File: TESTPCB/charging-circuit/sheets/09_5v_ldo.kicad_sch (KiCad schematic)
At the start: 8 parts, among them P6 1.27mm/1*3p, U2 MT3608

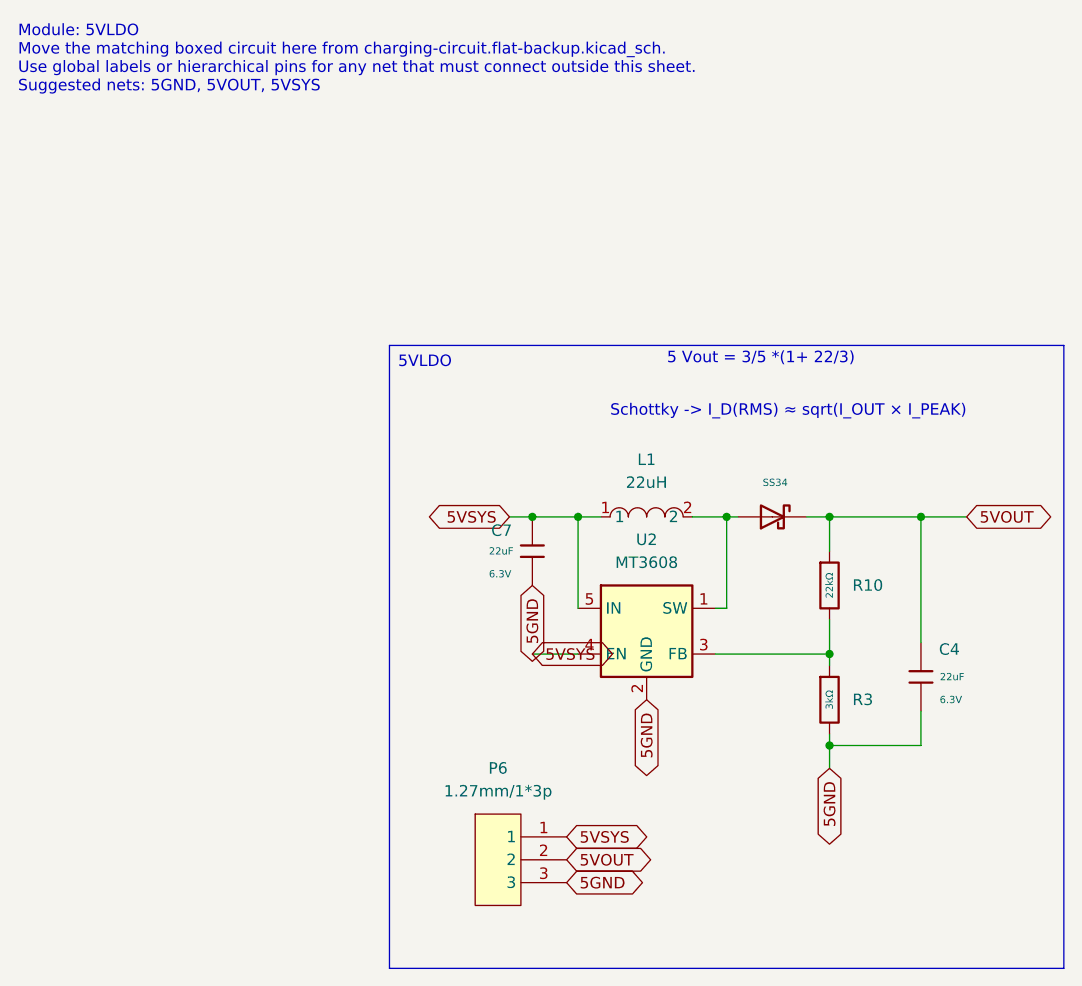
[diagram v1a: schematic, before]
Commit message: Fixed formatting issues, now the hierachal sheets are all labeled as net labels and when we want to expose their pins we will make them into hierchal or global pins
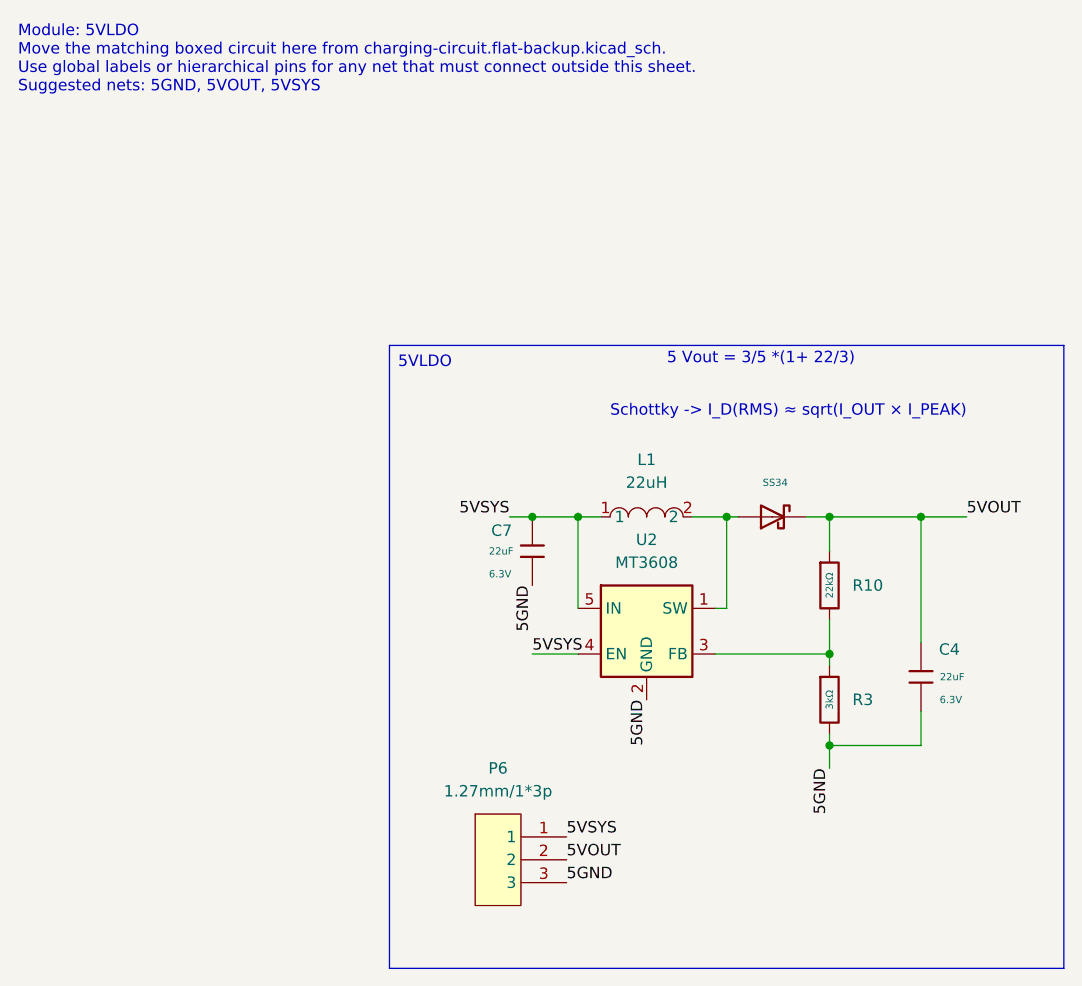
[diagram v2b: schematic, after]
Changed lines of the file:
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@@
 		)
 	)
-	(global_label "5VSYS"
-		(shape bidirectional)
+	(label "5VSYS"
 		(at 86.36 111.76 0)
 		(effects
@@
 			(justify left bottom)
 		)
-		(property "Intersheetrefs" "${INTERSHEET_REFS}"
-			(at 86.36 111.76 0)
-			(effects
-				(font
-					(size 1.27 1.27)
-				)
-				(hide yes)
-			)
-		)
 	)
-	(global_label "5VSYS"
-		(shape bidirectional)
+	(label "5VSYS"
 		(at 82.55 91.44 0)
 		(effects
@@
 			(justify left bottom)
 		)
-		(property "Intersheetrefs" "${INTERSHEET_REFS}"
-			(at 82.55 91.44 0)
-			(effects
-				(font
-					(size 1.27 1.27)
-				)
-				(hide yes)
-			)
-		)
 	)
-	(global_label "5VOUT"
-		(shape bidirectional)
+	(label "5VOUT"
 		(at 86.36 114.3 0)
 		(effects
@@
 			(justify left bottom)
 		)
-		(property "Intersheetrefs" "${INTERSHEET_REFS}"
-			(at 86.36 114.3 0)
-			(effects
-				(font
-					(size 1.27 1.27)
-				)
-				(hide yes)
-			)
-		)
 	)
-	(global_label "5GND"
-		(shape bidirectional)
+	(label "5GND"
 		(at 82.55 83.82 270)
 		(effects
@@
 			(justify right bottom)
 		)
-		(property "Intersheetrefs" "${INTERSHEET_REFS}"
-			(at 82.55 83.82 0)
-			(effects
-				(font
-					(size 1.27 1.27)
-				)
-				(hide yes)
-			)
-		)
 	)
-	(global_label "5VSYS"
-		(shape bidirectional)
+	(label "5VSYS"
 		(at 80.01 76.2 180)
 		(effects
@@
 			(justify right bottom)
 		)
-		(property "Intersheetrefs" "${INTERSHEET_REFS}"
-			(at 80.01 76.2 0)
-			(effects
-				(font
-					(size 1.27 1.27)
-				)
-				(hide yes)
-			)
-		)
 	)
-	(global_label "5GND"
-		(shape bidirectional)
+	(label "5GND"
 		(at 115.57 104.14 270)
 		(effects
@@
 			(justify right bottom)
 		)
-		(property "Intersheetrefs" "${INTERSHEET_REFS}"
-			(at 115.57 104.14 0)
-			(effects
-				(font
-					(size 1.27 1.27)
-				)
-				(hide yes)
-			)
-		)
 	)
-	(global_label "5VOUT"
-		(shape bidirectional)
+	(label "5VOUT"
 		(at 130.81 76.2 0)
 		(effects
@@
 			(justify left bottom)
 		)
-		(property "Intersheetrefs" "${INTERSHEET_REFS}"
-			(at 130.81 76.2 0)
-			(effects
-				(font
-					(size 1.27 1.27)
-				)
-				(hide yes)
-			)
-		)
 	)
-	(global_label "5GND"
-		(shape bidirectional)
+	(label "5GND"
 		(at 95.25 96.52 270)
 		(effects
@@
 			(justify right bottom)
 		)
-		(property "Intersheetrefs" "${INTERSHEET_REFS}"
-			(at 95.25 96.52 0)
-			(effects
-				(font
-					(size 1.27 1.27)
-				)
-				(hide yes)
-			)
-		)
 	)
-	(global_label "5GND"
-		(shape bidirectional)
+	(label "5GND"
 		(at 86.36 116.84 0)
 		(effects
@@
 			(justify left bottom)
 		)
-		(property "Intersheetrefs" "${INTERSHEET_REFS}"
-			(at 86.36 116.84 0)
-			(effects
-				(font
-					(size 1.27 1.27)
-				)
-				(hide yes)
-			)
-		)
 	)
